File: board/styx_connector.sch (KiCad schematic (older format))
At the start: 3 parts, among them J4 Styx_P4, J5 Styx_P5, J6 Conn_02x12_Odd_Even

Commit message: Board: Basic layout done, but need to make the board longer to avoid mechanical conflict with the monitor
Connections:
- net DBG1: now also J4.13 (H20); no longer J4.5 (J22)
- net DBG10: now also J4.11 (G21), J6.12 (Pin_12); no longer J4.22 (D22), J6.21 (Pin_21)
- net DBG11: now also J4.18 (F21), J6.13 (Pin_13); no longer J4.7 (L22), J6.4 (Pin_4)
- net DBG12: now also J4.12 (G20), J6.14 (Pin_14); no longer J4.11 (G21), J6.6 (Pin_6)
- net DBG13: now also J4.22 (D22), J6.15 (Pin_15); no longer J4.8 (L21), J6.8 (Pin_8)
- net DBG14: now also J4.21 (C22), J6.16 (Pin_16); no longer J4.12 (G20), J6.10 (Pin_10)
- net DBG15: now also J5.15 (N19), J6.17 (Pin_17); no longer J5.7 (M19), J6.12 (Pin_12)
- net DBG16: now also J6.18 (Pin_18); no longer J6.14 (Pin_14)
- net DBG17: now also J5.7 (M19), J6.19 (Pin_19); no longer J5.15 (N19), J6.16 (Pin_16)
- net DBG18: now also J5.16 (N20), J6.20 (Pin_20); no longer J5.8 (M20), J6.18 (Pin_18)
- net DBG19: now also J6.21 (Pin_21); no longer J6.20 (Pin_20)
- net DBG2: now also J4.17 (F22), J6.4 (Pin_4); no longer J4.9 (G22), J6.5 (Pin_5)
- net DBG20: now also J5.8 (M20); no longer J5.16 (N20)
- net DBG3: now also J4.5 (J22), J6.5 (Pin_5); no longer J4.13 (H20), J6.7 (Pin_7)
- net DBG4: now also J4.9 (G22), J6.6 (Pin_6); no longer J4.17 (F22), J6.9 (Pin_9)
- net DBG5: now also J4.14 (H19), J6.7 (Pin_7); no longer J4.21 (C22), J6.11 (Pin_11)
- net DBG6: now also J6.8 (Pin_8); no longer J6.13 (Pin_13)
- net DBG7: now also J6.9 (Pin_9); no longer J6.15 (Pin_15)
- net DBG8: now also J4.7 (L22), J6.10 (Pin_10); no longer J4.14 (H19), J6.17 (Pin_17)
- net DBG9: now also J4.8 (L21), J6.11 (Pin_11); no longer J4.18 (F21), J6.19 (Pin_19)
- net +3V3_FPGA: now reaches J4.93 (3V3)
- net +3V3_FPGA: now also J4.94 (3V3), J4.95 (3V3), J4.96 (3V3), J5.90 (3V3), J5.92 (3V3)
- no-connect marks 18 -> 12
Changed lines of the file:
@@
-$Comp
-L agc_monitor:Styx_P4 J4
-U 1 1 5C9E4962
-P 3250 2100
-F 0 "J4" H 3275 3383 50  0000 C CNN
-F 1 "Styx_P4" H 3275 3384 50  0001 C CNN
-F 2 "agc_monitor:PinHeader_4x24_P2.54mm_Vertical" H 3600 2100 50  0001 C CNN
-F 3 "" H 3600 2100 50  0001 C CNN
-	1    3250 2100
-	1    0    0    -1
-$EndComp
 $Comp
 L agc_monitor:Styx_P4 J4
@@
 	3850 1550 3800 1550
 Wire Wire Line
+	2750 1250 2500 1250
+Text Label 2500 1250 0    50   ~ 0
+DBG1
+Wire Wire Line
+	2750 1350 2500 1350
+Text Label 2500 1350 0    50   ~ 0
+DBG2
+Wire Wire Line
 	2750 1050 2500 1050
 Text Label 2500 1050 0    50   ~ 0
-DBG1
+DBG3
 Wire Wire Line
 	2750 1150 2500 1150
 Text Label 2500 1150 0    50   ~ 0
-DBG2
-Wire Wire Line
-	2750 1250 2500 1250
-Text Label 2500 1250 0    50   ~ 0
-DBG3
-Wire Wire Line
-	2750 1350 2500 1350
-Text Label 2500 1350 0    50   ~ 0
 DBG4
 Wire Wire Line
-	2750 1450 2500 1450
-Text Label 2500 1450 0    50   ~ 0
+	3800 1250 4050 1250
+Text Label 4050 1250 2    50   ~ 0
 DBG5
 Wire Wire Line
@@
 DBG7
 Wire Wire Line
-	3800 1250 4050 1250
-Text Label 4050 1250 2    50   ~ 0
+	6050 1050 5800 1050
+Text Label 5800 1050 0    50   ~ 0
 DBG8
 Wire Wire Line
-	3800 1350 4050 1350
-Text Label 4050 1350 2    50   ~ 0
+	7100 1050 7350 1050
+Text Label 7350 1050 2    50   ~ 0
 DBG9
+Wire Wire Line
+	6050 1150 5750 1150
+Text Label 5750 1150 0    50   ~ 0
+DBG10
+Wire Wire Line
+	3800 1350 4100 1350
+Text Label 4100 1350 2    50   ~ 0
+DBG11
+Wire Wire Line
+	7100 1150 7400 1150
+Text Label 7400 1150 2    50   ~ 0
+DBG12
 Wire Wire Line
 	3800 1450 4100 1450
 Text Label 4100 1450 2    50   ~ 0
-DBG10
-Wire Wire Line
-	6050 1050 5750 1050
-Text Label 5750 1050 0    50   ~ 0
-DBG11
-Wire Wire Line
-	6050 1150 5750 1150
-Text Label 5750 1150 0    50   ~ 0
-DBG12
-Wire Wire Line
-	7100 1050 7400 1050
-Text Label 7400 1050 2    50   ~ 0
 DBG13
 Wire Wire Line
-	7100 1150 7400 1150
-Text Label 7400 1150 2    50   ~ 0
+	2750 1450 2450 1450
+Text Label 2450 1450 0    50   ~ 0
 DBG14
 Wire Wire Line
-	6050 3850 5750 3850
-Text Label 5750 3850 0    50   ~ 0
+	6050 4050 5750 4050
+Text Label 5750 4050 0    50   ~ 0
 DBG15
 Wire Wire Line
@@
 DBG16
 Wire Wire Line
-	6050 4050 5750 4050
-Text Label 5750 4050 0    50   ~ 0
+	6050 3850 5750 3850
+Text Label 5750 3850 0    50   ~ 0
 DBG17
 Wire Wire Line
-	7100 3850 7400 3850
-Text Label 7400 3850 2    50   ~ 0
+	7100 4050 7400 4050
+Text Label 7400 4050 2    50   ~ 0
 DBG18
 Wire Wire Line
@@
 DBG19
 Wire Wire Line
-	7100 4050 7400 4050
-Text Label 7400 4050 2    50   ~ 0
+	7100 3850 7400 3850
+Text Label 7400 3850 2    50   ~ 0
 DBG20
 Wire Wire Line
@@
 DBG_3V3
 NoConn ~ 6050 3750
-NoConn ~ 7100 5950
-NoConn ~ 3800 5950
-NoConn ~ 7100 3250
-NoConn ~ 3800 3250
-NoConn ~ 2750 3250
-NoConn ~ 6050 3250
 $Comp
 L Connector_Generic:Conn_02x12_Odd_Even J6
@@
 DBG1
 Wire Wire Line
+	9250 1350 9500 1350
+Text Label 9500 1350 2    50   ~ 0
+DBG2
+Wire Wire Line
 	8750 1450 8500 1450
 Text Label 8500 1450 0    50   ~ 0
-DBG2
+DBG3
+Wire Wire Line
+	9250 1450 9500 1450
+Text Label 9500 1450 2    50   ~ 0
+DBG4
 Wire Wire Line
 	8750 1550 8500 1550
 Text Label 8500 1550 0    50   ~ 0
-DBG3
+DBG5
+Wire Wire Line
+	9250 1550 9500 1550
+Text Label 9500 1550 2    50   ~ 0
+DBG6
 Wire Wire Line
 	8750 1650 8500 1650
 Text Label 8500 1650 0    50   ~ 0
-DBG4
+DBG7
+Wire Wire Line
+	9250 1650 9500 1650
+Text Label 9500 1650 2    50   ~ 0
+DBG8
 Wire Wire Line
 	8750 1750 8500 1750
 Text Label 8500 1750 0    50   ~ 0
-DBG5
-Wire Wire Line
-	8750 1850 8500 1850
-Text Label 8500 1850 0    50   ~ 0
-DBG6
-Wire Wire Line
-	8750 1950 8500 1950
-Text Label 8500 1950 0    50   ~ 0
-DBG7
-Wire Wire Line
-	8750 2050 8500 2050
-Text Label 8500 2050 0    50   ~ 0
-DBG8
-Wire Wire Line
-	8750 2150 8500 2150
-Text Label 8500 2150 0    50   ~ 0
 DBG9
+Wire Wire Line
+	9250 1750 9550 1750
+Text Label 9550 1750 2    50   ~ 0
+DBG10
+Wire Wire Line
+	8750 1850 8450 1850
+Text Label 8450 1850 0    50   ~ 0
+DBG11
+Wire Wire Line
+	9250 1850 9550 1850
+Text Label 9550 1850 2    50   ~ 0
+DBG12
+Wire Wire Line
+	8750 1950 8450 1950
+Text Label 8450 1950 0    50   ~ 0
+DBG13
+Wire Wire Line
+	9250 1950 9550 1950
+Text Label 9550 1950 2    50   ~ 0
+DBG14
+Wire Wire Line
+	8750 2050 8450 2050
+Text Label 8450 2050 0    50   ~ 0
+DBG15
+Wire Wire Line
+	9250 2050 9550 2050
+Text Label 9550 2050 2    50   ~ 0
+DBG16
+Wire Wire Line
+	8750 2150 8450 2150
+Text Label 8450 2150 0    50   ~ 0
+DBG17
+Wire Wire Line
+	9250 2150 9550 2150
+Text Label 9550 2150 2    50   ~ 0
+DBG18
 Wire Wire Line
 	8750 2250 8450 2250
 Text Label 8450 2250 0    50   ~ 0
-DBG10
-Wire Wire Line
-	9250 1350 9550 1350
-Text Label 9550 1350 2    50   ~ 0
-DBG11
-Wire Wire Line
-	9250 1450 9550 1450
-Text Label 9550 1450 2    50   ~ 0
-DBG12
-Wire Wire Line
-	9250 1550 9550 1550
-Text Label 9550 1550 2    50   ~ 0
-DBG13
-Wire Wire Line
-	9250 1650 9550 1650
-Text Label 9550 1650 2    50   ~ 0
-DBG14
-Wire Wire Line
-	9250 1750 9550 1750
-Text Label 9550 1750 2    50   ~ 0
-DBG15
-Wire Wire Line
-	9250 1850 9550 1850
-Text Label 9550 1850 2    50   ~ 0
-DBG16
-Wire Wire Line
-	9250 1950 9550 1950
-Text Label 9550 1950 2    50   ~ 0
-DBG17
-Wire Wire Line
-	9250 2050 9550 2050
-Text Label 9550 2050 2    50   ~ 0
-DBG18
-Wire Wire Line
-	9250 2150 9550 2150
-Text Label 9550 2150 2    50   ~ 0
 DBG19
 Wire Wire Line
@@
 Wire Wire Line
 	9000 2450 9300 2450
+$Comp
+L agc_monitor:Styx_P4 J4
+U 1 1 5C9E4962
+P 3250 2100
+F 0 "J4" H 3275 3383 50  0000 C CNN
+F 1 "Styx_P4" H 3275 3384 50  0001 C CNN
+F 2 "agc_monitor:PinHeader_4x24_P2.54mm_Vertical" H 3600 2100 50  0001 C CNN
+F 3 "" H 3600 2100 50  0001 C CNN
+	1    3250 2100
+	1    0    0    -1
+$EndComp
+Wire Wire Line
+	2750 3250 2700 3250
+Wire Wire Line
+	2700 3250 2700 3550
+Wire Wire Line
+	2700 3550 3300 3550
+Wire Wire Line
+	3850 3550 3850 3250
+Wire Wire Line
+	3850 3250 3800 3250
+$Comp
+L agc_monitor:+3V3_FPGA #PWR0188
+U 1 1 5D1611E0
+P 3300 3550
+F 0 "#PWR0188" H 3300 3400 50  0001 C CNN
+F 1 "+3V3_FPGA" H 3285 3723 50  0000 C CNN
+F 2 "" H 3300 3550 50  0001 C CNN
+F 3 "" H 3300 3550 50  0001 C CNN
+	1    3300 3550
+	1    0    0    -1
+$EndComp
+Connection ~ 3300 3550
+Wire Wire Line
+	3300 3550 3850 3550
+Wire Wire Line
+	6000 3250 6000 3550
+Wire Wire Line
+	6000 3550 6600 3550
+Wire Wire Line
+	7150 3550 7150 3250
+$Comp
+L agc_monitor:+3V3_FPGA #PWR0189
+U 1 1 5D162096
+P 6600 3550
+F 0 "#PWR0189" H 6600 3400 50  0001 C CNN
+F 1 "+3V3_FPGA" H 6585 3723 50  0000 C CNN
+F 2 "" H 6600 3550 50  0001 C CNN
+F 3 "" H 6600 3550 50  0001 C CNN
+	1    6600 3550
+	1    0    0    -1
+$EndComp
+Connection ~ 6600 3550
+Wire Wire Line
+	6600 3550 7150 3550
+Wire Wire Line
+	6050 3250 6000 3250
+Wire Wire Line
+	7100 3250 7150 3250
+Wire Wire Line
+	3800 5950 4650 5950
+Wire Wire Line
+	4650 5950 4650 5850
+$Comp
+L agc_monitor:+3V3_FPGA #PWR0190
+U 1 1 5D20B833
+P 4650 5850
+F 0 "#PWR0190" H 4650 5700 50  0001 C CNN
+F 1 "+3V3_FPGA" H 4635 6023 50  0000 C CNN
+F 2 "" H 4650 5850 50  0001 C CNN
+F 3 "" H 4650 5850 50  0001 C CNN
+	1    4650 5850
+	1    0    0    -1
+$EndComp
+Wire Wire Line
+	7100 5950 7950 5950
+Wire Wire Line
+	7950 5950 7950 5850
+$Comp
+L agc_monitor:+3V3_FPGA #PWR0191
+U 1 1 5D23C506
+P 7950 5850
+F 0 "#PWR0191" H 7950 5700 50  0001 C CNN
+F 1 "+3V3_FPGA" H 7935 6023 50  0000 C CNN
+F 2 "" H 7950 5850 50  0001 C CNN
+F 3 "" H 7950 5850 50  0001 C CNN
+	1    7950 5850
+	1    0    0    -1
+$EndComp
 $EndSCHEMATC

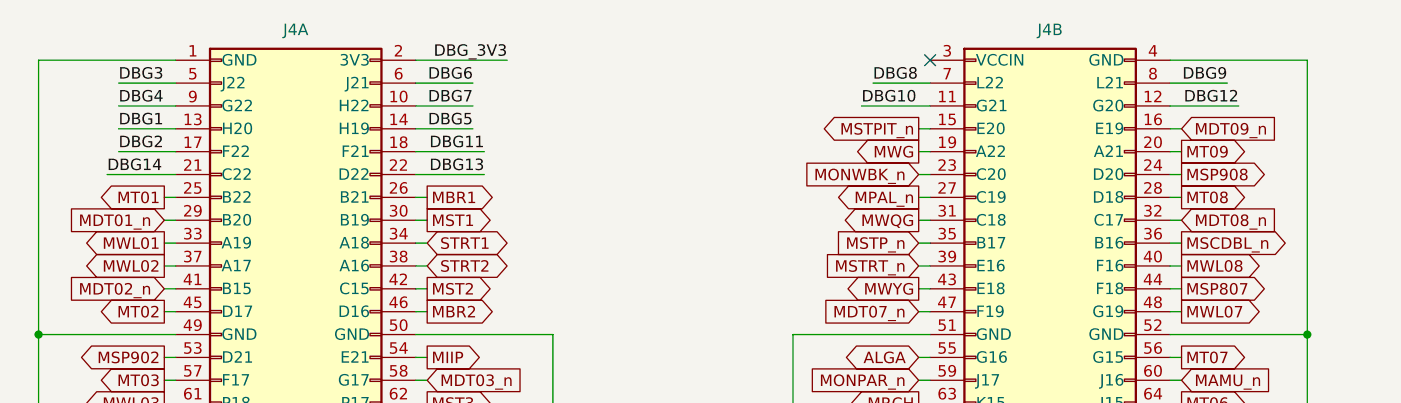
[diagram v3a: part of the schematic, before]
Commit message: Board: finished routing of extended board
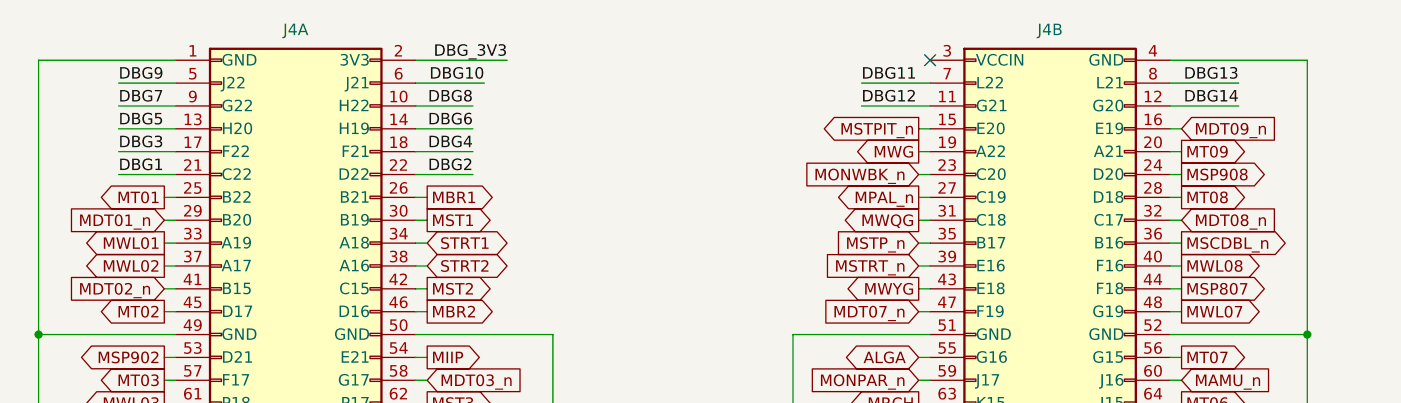
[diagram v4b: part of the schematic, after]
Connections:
- net DBG1: now also J4.21 (C22); no longer J4.13 (H20)
- net DBG10: now also J4.6 (J21); no longer J4.11 (G21)
- net DBG11: now also J4.7 (L22); no longer J4.18 (F21)
- net DBG12: now also J4.11 (G21); no longer J4.12 (G20)
- net DBG13: now also J4.8 (L21); no longer J4.22 (D22)
- net DBG14: now also J4.12 (G20); no longer J4.21 (C22)
- net DBG2: now also J4.22 (D22); no longer J4.17 (F22)
- net DBG3: now also J4.17 (F22); no longer J4.5 (J22)
- net DBG4: now also J4.18 (F21); no longer J4.9 (G22)
- net DBG5: now also J4.13 (H20); no longer J4.14 (H19)
- net DBG6: now also J4.14 (H19); no longer J4.6 (J21)
- net DBG7: now also J4.9 (G22); no longer J4.10 (H22)
- net DBG8: now also J4.10 (H22); no longer J4.7 (L22)
- net DBG9: now also J4.5 (J22); no longer J4.8 (L21)
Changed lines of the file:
@@
 	3850 1550 3800 1550
+Wire Wire Line
+	2750 1450 2500 1450
+Text Label 2500 1450 0    50   ~ 0
+DBG1
+Wire Wire Line
+	3800 1450 4050 1450
+Text Label 4050 1450 2    50   ~ 0
+DBG2
+Wire Wire Line
+	2750 1350 2500 1350
+Text Label 2500 1350 0    50   ~ 0
+DBG3
+Wire Wire Line
+	3800 1350 4050 1350
+Text Label 4050 1350 2    50   ~ 0
+DBG4
 Wire Wire Line
 	2750 1250 2500 1250
 Text Label 2500 1250 0    50   ~ 0
-DBG1
+DBG5
 Wire Wire Line
-	2750 1350 2500 1350
-Text Label 2500 1350 0    50   ~ 0
-DBG2
+	3800 1250 4050 1250
+Text Label 4050 1250 2    50   ~ 0
+DBG6
+Wire Wire Line
+	2750 1150 2500 1150
+Text Label 2500 1150 0    50   ~ 0
+DBG7
+Wire Wire Line
+	3800 1150 4050 1150
+Text Label 4050 1150 2    50   ~ 0
+DBG8
 Wire Wire Line
 	2750 1050 2500 1050
 Text Label 2500 1050 0    50   ~ 0
-DBG3
+DBG9
 Wire Wire Line
-	2750 1150 2500 1150
-Text Label 2500 1150 0    50   ~ 0
-DBG4
+	3800 1050 4100 1050
+Text Label 4100 1050 2    50   ~ 0
+DBG10
 Wire Wire Line
-	3800 1250 4050 1250
-Text Label 4050 1250 2    50   ~ 0
-DBG5
-Wire Wire Line
-	3800 1050 4050 1050
-Text Label 4050 1050 2    50   ~ 0
-DBG6
-Wire Wire Line
-	3800 1150 4050 1150
-Text Label 4050 1150 2    50   ~ 0
-DBG7
-Wire Wire Line
-	6050 1050 5800 1050
-Text Label 5800 1050 0    50   ~ 0
-DBG8
-Wire Wire Line
-	7100 1050 7350 1050
-Text Label 7350 1050 2    50   ~ 0
-DBG9
+	6050 1050 5750 1050
+Text Label 5750 1050 0    50   ~ 0
+DBG11
 Wire Wire Line
 	6050 1150 5750 1150
 Text Label 5750 1150 0    50   ~ 0
-DBG10
+DBG12
 Wire Wire Line
-	3800 1350 4100 1350
-Text Label 4100 1350 2    50   ~ 0
-DBG11
+	7100 1050 7400 1050
+Text Label 7400 1050 2    50   ~ 0
+DBG13
 Wire Wire Line
 	7100 1150 7400 1150
 Text Label 7400 1150 2    50   ~ 0
-DBG12
-Wire Wire Line
-	3800 1450 4100 1450
-Text Label 4100 1450 2    50   ~ 0
-DBG13
-Wire Wire Line
-	2750 1450 2450 1450
-Text Label 2450 1450 0    50   ~ 0
 DBG14
 Wire Wire Line
